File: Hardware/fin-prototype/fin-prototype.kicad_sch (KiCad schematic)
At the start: 0 parts

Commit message: setup libraries
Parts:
- added C1, C2, C4: 10 nF, Capacitor_SMD:C_0603_1608Metric, symbol Device:C_Small
- added C3, C5: 1 uF, Capacitor_SMD:C_0603_1608Metric, symbol Device:C_Small
- added C6: 220 nF, Capacitor_SMD:C_0603_1608Metric, symbol Device:C_Small
- added J10, J9: Conn_01x04_Pin, Connector_PinHeader_2.54mm:PinHeader_1x04_P2.54mm_Vertical, symbol Connector:Conn_01x04_Pin
- added R1: 10 k, Resistor_SMD:R_0603_1608Metric, symbol Device:R_US
- added R2, R3, R8, R9: 1 k, Resistor_SMD:R_0603_1608Metric, symbol Device:R_US
- added R4, R5, R6, R7: 2.5 k, Resistor_SMD:R_0603_1608Metric, symbol Device:R_US
- added U1: ADS131M03QPWRQ1, FinLib:ADS131M03, symbol FinLib:ADS131M03QPWRQ1
- added U2: TMP235A4DBZR, FinLib:TMP235A4DBZR, symbol FinLib:TMP235A4DBZR
- added U3: STM32L412KBUx, Package_DFN_QFN:QFN-32-1EP_5x5mm_P0.5mm_EP3.45x3.45mm, symbol MCU_ST_STM32L4:STM32L412KBUx
- added U4: W25N512GVEIG, FinLib:WSON8_8x6_E_WIN, symbol FinLib:W25N512GVEIG
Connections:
- new net: C4.1, R6.2, U1.7 (AIN2P)
- new net: C4.2, R7.1, U1.8 (AIN2N)
- new net: C1.1, R1.2, U1.3 (AIN0P)
- new net: C2.1, R4.2, U1.5 (AIN1N)
- new net: C2.2, R5.1, U1.6 (AIN1P)
- new net: U3.16 (VSS), U3.32 (VSS), U3.33 (VSS)
- new net: C6.1, U1.18 (CAP)
- new net +3.3V: C3.1, C5.1, J10.1 (Pin_1), J9.1 (Pin_1), R2.2, R8.1, U1.1 (AVDD), U1.20 (DVDD), U2.1 (VDD)
- new net ADCCLK: U1.17 (CLKIN)
- new net DIN: U1.16 (DIN)
- new net DOUT: U1.15 (DOUT)
- new net GAUGE1_IN_N: R2.1, R3.1, R6.1
- new net GAUGE1_IN_P: J9.2 (Pin_2), J9.3 (Pin_3), R7.2
- new net GAUGE2_IN_N: R5.2, R8.2, R9.2
- new net GAUGE2_IN_P: J10.2 (Pin_2), J10.3 (Pin_3), R4.1
- new net GND: C1.2, C3.2, C5.2, C6.2, J10.4 (Pin_4), J9.4 (Pin_4), R3.2, R9.1, U1.19 (DGND), U1.2 (AGND), U1.4 (AIN0N), U2.3 (GND)
- new net SPICLK: U1.14 (SCLK)
- new net TMP_IN_P: R1.1, U2.2 (VOUT)
- new net ~{CS}: U1.12 (*CS)
- new net ~{DRDY}: U1.13 (*DRDY)
- new net ~{SYNC}/~{RST}: U1.11 (*SYNC/*RESET)

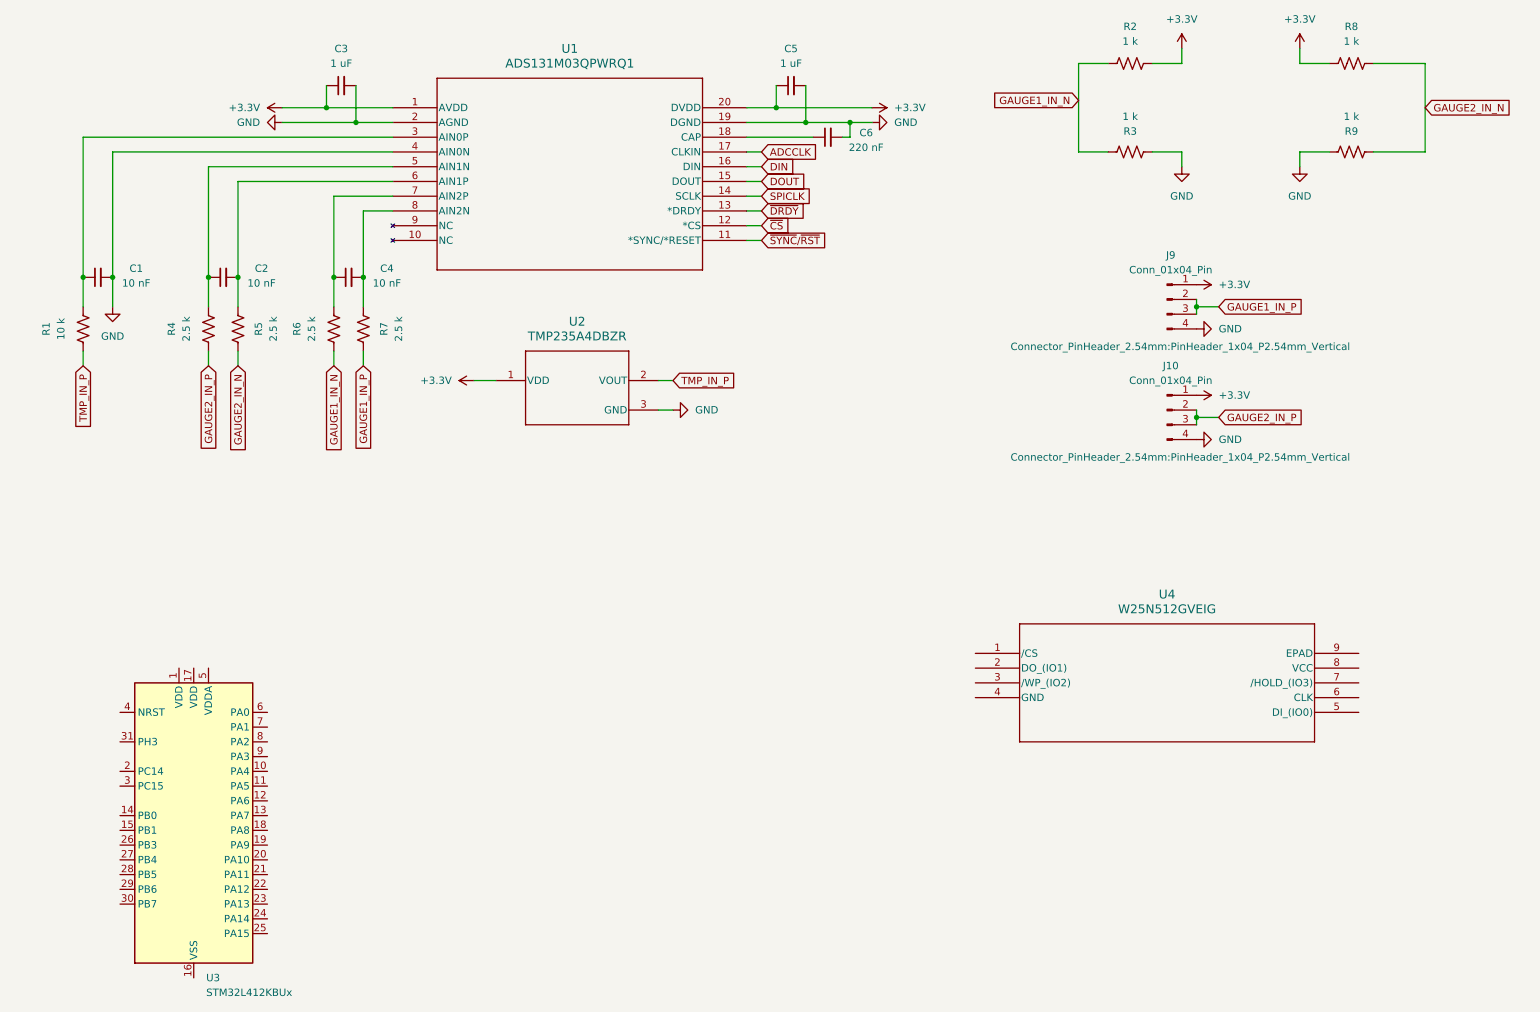
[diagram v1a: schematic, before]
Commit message: start pin assignments
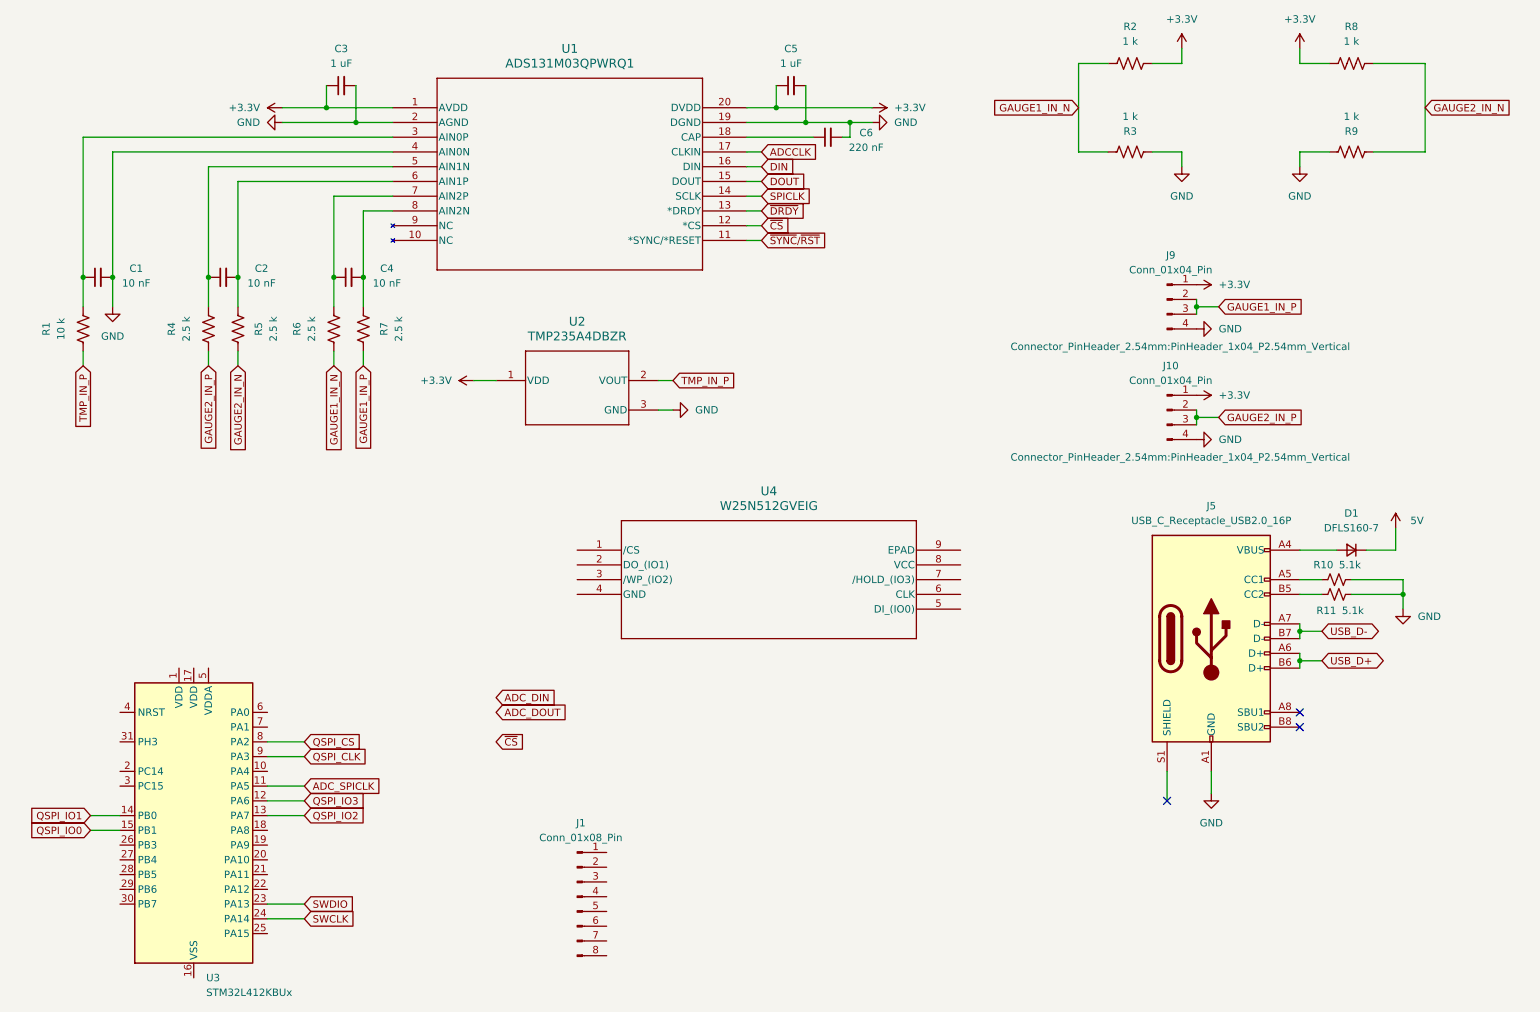
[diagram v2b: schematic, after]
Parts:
- added D1: DFLS160-7, Diode_SMD:D_PowerDI-123, symbol Device:D_Small
- added J1: Conn_01x08_Pin, symbol Connector:Conn_01x08_Pin
- added J5: USB_C_Receptacle_USB2.0_16P, Connector_USB:USB_C_Receptacle_GCT_USB4105-xx-A_16P_TopMnt_Horizontal, symbol Connector:USB_C_Receptacle_USB2.0_16P
- added R10, R11: 5.1k, Resistor_SMD:R_0402_1005Metric, symbol Device:R_Small_US
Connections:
- net GND: now also J5.A1 (GND), J5.A12 (GND), J5.B1 (GND), J5.B12 (GND), R10.2, R11.2
- net ADC_SPICLK: now reaches U3.11 (PA5)
- net QSPI_IO3: now reaches U3.12 (PA6)
- net QSPI_IO2: now reaches U3.13 (PA7)
- net QSPI_IO1: now reaches U3.14 (PB0)
- net QSPI_IO0: now reaches U3.15 (PB1)
- net SWDIO: now reaches U3.23 (PA13)
- net SWCLK: now reaches U3.24 (PA14)
- net QSPI_CS: now reaches U3.8 (PA2)
- net QSPI_CLK: now reaches U3.9 (PA3)
- new net: D1.2 (A), J5.A4 (VBUS), J5.A9 (VBUS), J5.B4 (VBUS), J5.B9 (VBUS)
- new net: J5.A5 (CC1), R10.1
- new net: J5.B5 (CC2), R11.1
- new net 5V: D1.1 (K)
- new net USB_D+: J5.A6 (D+), J5.B6 (D+)
- new net USB_D-: J5.A7 (D-), J5.B7 (D-)
- no-connect marks 0 -> 3
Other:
- moved on the sheet: U4

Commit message: finished schematic
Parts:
- removed U3: STM32L412KBUx, Package_DFN_QFN:QFN-32-1EP_5x5mm_P0.5mm_EP3.45x3.45mm, symbol MCU_ST_STM32L4:STM32L412KBUx
- added C10, C11, C12, C7, C8, C9: 100nF, Capacitor_SMD:C_0603_1608Metric, symbol Device:C_Small
- added D2, D3, D4, D5: LED, LED_SMD:LED_0603_1608Metric, symbol Device:LED
- added J2: Conn_01x04_Pin, FinLib:FlexCable, symbol Connector:Conn_01x04_Pin
- added R12, R13, R14, R15: 220 Ohms, Resistor_SMD:R_0603_1608Metric, symbol Device:R_Small_US
- added R16: 5K, Resistor_SMD:R_0603_1608Metric, symbol Device:R_Small_US
- added SW1, SW2: SW_Push, FinLib:SW_FSM2JMTR_TEC, symbol Switch:SW_Push
- added TP1, TP10, TP11, TP12, TP13, TP14, TP2, TP3, TP4, TP5, TP6, TP7, TP8, TP9: TestPoint, FinLib:TestPoint, symbol Connector:TestPoint
- added U3: FT232RNQ-REEL, FinLib:QFN32_FT232_FTD, symbol FinLib:FT232RNQ-REEL
- added U5: STM32L412C8T6, FinLib:LQFP-48, symbol FinLib:STM32L412C8T6
- J1: footprint (none) -> Connector_PinHeader_2.54mm:PinHeader_1x08_P2.54mm_Horizontal
- R10, R11: footprint Resistor_SMD:R_0402_1005Metric -> Resistor_SMD:R_0603_1608Metric
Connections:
- net DIN is gone; now on net ADC_DIN: U1.16 (DIN)
- net DOUT is gone; now on net ADC_DOUT: U1.15 (DOUT)
- net SPICLK is gone; now on net ADC_SPICLK: U1.14 (SCLK)
- net +3.3V: now also J1.7 (Pin_7), U4.8 (VCC), C10.1, C12.1, C8.2, C9.2, D4.2 (A), J2.1 (Pin_1), R12.2, R13.2, SW2.2, U3.1 (VCCIO), U5.1 (VBAT), U5.24 (VDDA/VREF+), U5.48 (VDD), U5.9 (VDDA/VREF+)
- net ADC_DIN: now also TP14.1, U5.28 (PB15)
- net ADC_DOUT: now also TP13.1, U5.27 (PB14)
- net ADC_SPICLK: now also TP12.1, U5.26 (PB13)
- net GND: now also J1.8 (Pin_8), U4.4 (GND), U4.9 (EPAD), C10.2, C11.2, C12.2, C7.2, C8.1, C9.1, J2.4 (Pin_4), R14.2, R15.2, R16.2, SW1.2, U3.17 (GND), U3.20 (GND), U3.24 (AGND), U3.26 (TEST), U3.33 (EPAD), U3.4 (GND), U5.23 (VSSA/VREF-), U5.35 (VSS), U5.47 (VSS), U5.8 (VSSA/VREF-)
- net QSPI_CLK: now also U4.6 (CLK), TP5.1, U5.13 (PA3)
- net QSPI_CS: now also U4.1 (/CS), TP4.1, U5.12 (PA2)
- net QSPI_IO0: now also U4.5 (DI_(IO0)), TP8.1, U5.19 (PB1)
- net QSPI_IO1: now also U4.2 (DO_(IO1)), TP7.1, U5.18 (PB0)
- net QSPI_IO2: now also U4.3 (/WP_(IO2)), TP6.1, U5.17 (PA7)
- net QSPI_IO3: now also U4.7 (/HOLD_(IO3)), U5.16 (PA6)
- net SWCLK: now also J1.4 (Pin_4), U5.37 (PA14)
- net SWDIO: now also J1.5 (Pin_5), U5.34 (PA13)
- net USB_D+: now also U3.14 (USBDP)
- net USB_D-: now also U3.15 (USBDM)
- net DATA_MOSI: now reaches J1.1 (Pin_1)
- net DATA_MOSI: now also U5.33 (PA12)
- net DATA_MISO: now reaches J1.2 (Pin_2)
- net DATA_MISO: now also U5.32 (PA11)
- net DATA_CS: now reaches J1.3 (Pin_3)
- net DATA_CS: now also U5.14 (PA4)
- net DATA_SCK: now reaches J1.6 (Pin_6)
- net DATA_SCK: now also U5.11 (PA1)
- net 5V renamed +5V
- net +5V: now also U3.19 (VCC)
- net ADCCLK renamed ADC_CLK
- net ADC_CLK: now also TP3.1, U5.10 (PA0)
- net ~{CS} renamed ADC_~{CS}
- net ADC_~{CS}: now also TP11.1, U5.25 (PB12)
- net ~{DRDY} renamed ADC_~{DRDY}
- net ADC_~{DRDY}: now also TP9.1, U5.45 (PB8)
- net ~{SYNC}/~{RST} renamed ADC_~{SYNC}/~{RST}
- net ADC_~{SYNC}/~{RST}: now also TP10.1, U5.46 (PB9)
- new net: C11.1, SW1.1, U5.7 (NRST)
- new net: D5.2 (A), U5.41 (PB5)
- new net: R16.1, SW2.1, U5.44 (PH3-BOOT0)
- new net: D4.1 (K), R14.1
- new net: D5.1 (K), R15.1
- new net: D2.1 (K), U3.22 (CBUS0)
- new net: D2.2 (A), R12.1
- new net: C7.1, U3.16 (3V3OUT)
- new net: D3.1 (K), U3.21 (CBUS1)
- new net: D3.2 (A), R13.1
- new net AVBAY_SYNC: J2.3 (Pin_3), U5.22 (PB11)
- new net PA15: U5.38 (PA15)
- new net PA5: U5.15 (PA5)
- new net PA8: U5.29 (PA8)
- new net PB2: U5.20 (PB2)
- new net PB3: U5.39 (PB3)
- new net PB4: U5.40 (PB4)
- new net PB6: U5.42 (PB6)
- new net PB7: U5.43 (PB7)
- new net PC13: U5.2 (PC13)
- new net PC14: U5.3 (PC14-OSC32_IN)
- new net PC15: U5.4 (PC15-OSC32_OUT)
- new net PH0: U5.5 (PH0-OSC_IN)
- new net PH1: U5.6 (PH1-OSC_OUT)
- new net SIGNAL: J2.2 (Pin_2), U5.21 (PB10)
- new net USART_RX: TP2.1, U3.30 (TXD), U5.31 (PA10)
- new net USART_TX: TP1.1, U3.2 (RXD), U5.30 (PA9)
- no-connect marks 3 -> 16
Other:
- note added: "Note: CLK uses TIM2_CH1 pin, ensure ETR pins aren't needed for anything"
- note added: "Potentially Change Strain Gauge to JST"
- moved on the sheet: C1, C2, C3, C4, C5, C6, D1, J1, J10, J5, J9, R1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

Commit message: prettify schematic a bit
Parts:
- removed C10, C11: 100nF, Capacitor_SMD:C_0603_1608Metric, symbol Device:C_Small
- removed D5: LED, LED_SMD:LED_0603_1608Metric, symbol Device:LED
- removed R13, R15: 220 Ohms, Resistor_SMD:R_0603_1608Metric, symbol Device:R_Small_US
- removed R16: 5K, Resistor_SMD:R_0603_1608Metric, symbol Device:R_Small_US
- removed U5: STM32L412C8T6, FinLib:LQFP-48, symbol FinLib:STM32L412C8T6
- added C2, C6, C7: 100nF, Capacitor_SMD:C_0603_1608Metric, symbol Device:C_Small
- added D4: LED, LED_SMD:LED_0603_1608Metric, symbol Device:LED
- added J10, J11, J12, J13, J14, J15, J16, J17, J18, J6, J7, J8, J9: Conn_01x01_Pin, Connector_PinHeader_2.54mm:PinHeader_1x01_P2.54mm_Vertical, symbol Connector:Conn_01x01_Pin
- added R10, R9: 220, Resistor_SMD:R_0603_1608Metric, symbol Device:R_Small_US
- added R2: 5K, Resistor_SMD:R_0603_1608Metric, symbol Device:R_Small_US
- added TP15, TP16, TP17, TP18, TP19, TP20, TP21: TestPoint, FinLib:TestPoint, symbol Connector:TestPoint
- added U2: STM32L412C8Tx, Package_QFP:LQFP-48_7x7mm_P0.5mm, symbol MCU_ST_STM32L4:STM32L412C8Tx
- R7: renamed from R14; value 220 Ohms -> 220
- R8: renamed from R12; value 220 Ohms -> 220
- TP1, TP2, TP3, TP4: footprint FinLib:TestPoint -> TestPoint:TestPoint_Loop_D1.80mm_Drill1.0mm_Beaded
- renumbered C5 to C10, C6 to C11, C7 to C13, C2 to C3, C3 to C4, C4 to C5, D4 to D1, D1 to D5, J5 to J1, J9 to J2, J10 to J3, J1 to J4, J2 to J5, R2 to R11, R3 to R12, R8 to R13, R9 to R14, R10 to R15, R11 to R16, R4 to R3, R5 to R4, R6 to R5, R7 to R6, U4 to U3, U2 to U4, U3 to U5
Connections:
- net DATA_SCK is gone; now on net SWCLK: J4.6 (Pin_6)
- net +3.3V: now also C4.2, C8.1, C9.1, D2.2 (A), D3.2 (A), SW2.1, C6.1, C7.1, U2.1 (VBAT), U2.24 (VDD), U2.48 (VDD), U2.9 (VDDA); no longer C4.1, C8.2, C9.2, R8.2, SW2.2
- net ADC_~{SYNC}/~{RST}: now also U2.46 (PB9)
- net AVBAY_SYNC: now also U2.22 (PB11)
- net GND: now also C4.1, C8.2, C9.2, SW1.1, TP1.1, TP2.1, TP3.1, TP4.1, C2.1, C6.2, C7.2, R10.1, R2.1, U2.23 (VSS), U2.35 (VSS), U2.47 (VSS), U2.8 (VSSA); no longer C4.2, C8.1, C9.1, SW1.2
- net PA15: now also J8.1 (Pin_1), U2.38 (PA15)
- net PA5: now also J6.1 (Pin_1), U2.15 (PA5)
- net PA8: now also J7.1 (Pin_1), U2.29 (PA8)
- net PB2: now also J9.1 (Pin_1), U2.20 (PB2)
- net PB3: now also J10.1 (Pin_1), U2.39 (PB3)
- net PB4: now also J11.1 (Pin_1), U2.40 (PB4)
- net PB6: now also J12.1 (Pin_1), U2.42 (PB6)
- net PB7: now also J13.1 (Pin_1), U2.43 (PB7)
- net PC13: now also J14.1 (Pin_1), U2.2 (PC13)
- net PC14: now also J15.1 (Pin_1), U2.3 (PC14)
- net PC15: now also J16.1 (Pin_1), U2.4 (PC15)
- net PH0: now also J17.1 (Pin_1), U2.5 (PH0)
- net PH1: now also J18.1 (Pin_1), U2.6 (PH1)
- net QSPI_CLK: now also TP12.1, U2.13 (PA3); no longer TP5.1
- net QSPI_IO0: now also TP13.1, U2.19 (PB1); no longer TP8.1
- net QSPI_IO1: now also TP14.1, U2.18 (PB0); no longer TP7.1
- net QSPI_IO2: now also TP15.1, U2.17 (PA7); no longer TP6.1
- net QSPI_IO3: now also TP16.1, U2.16 (PA6)
- net SIGNAL: now also U2.21 (PB10)
- net SWCLK: now also U2.37 (PA14); no longer J4.4 (Pin_4)
- net SWDIO: now also U2.34 (PA13)
- net USB_D+: now also TP20.1
- net USB_D-: now also TP21.1
- net at D2.1 (K): now also R8.2; no longer U5.22 (CBUS0)
- net ~{TX_LED}: now reaches R8.1
- net ~{TX_LED}: now also U5.22 (CBUS0); no longer D2.2 (A)
- net at D3.1 (K): now also R9.2; no longer U5.21 (CBUS1)
- net ADC_CLK renamed TIM2_CH1
- net TIM2_CH1: now also TP9.1, U2.10 (PA0); no longer TP3.1
- net ADC_DIN renamed SPI2_MOSI
- net SPI2_MOSI: now also TP7.1, U2.28 (PB15); no longer TP14.1
- net ADC_DOUT renamed SPI2_MISO
- net SPI2_MISO: now also TP6.1, U2.27 (PB14); no longer TP13.1
- net ADC_SPICLK renamed SPI2_SCK
- net SPI2_SCK: now also TP5.1, U2.26 (PB13); no longer TP12.1
- net ADC_~{CS} renamed ~{ADC_CS}
- net ~{ADC_CS}: now also TP8.1, U2.25 (PB12); no longer TP11.1
- net ADC_~{DRDY} renamed ~{ADC_DRDY}
- net ~{ADC_DRDY}: now also TP11.1, U2.45 (PB8); no longer TP9.1
- net DATA_CS renamed ~{SPI1_CS}
- net ~{SPI1_CS}: now also U2.14 (PA4)
- net DATA_MISO renamed SPI1_MISO
- net SPI1_MISO: now also U2.32 (PA11)
- net DATA_MOSI renamed SPI1_MOSI
- net SPI1_MOSI: now also U2.33 (PA12)
- net QSPI_CS renamed ~{FLASH_CS}
- net ~{FLASH_CS}: now also TP17.1, U2.12 (PA2); no longer TP4.1
- net USART_RX renamed USART1_RX
- net USART1_RX: now also TP18.1, U2.31 (PA10); no longer TP2.1
- net USART_TX renamed USART1_TX
- net USART1_TX: now also TP19.1, U2.30 (PA9); no longer TP1.1
- new net: D4.1 (K), R10.2
- new net: R2.2, SW2.2, U2.44 (PH3)
- new net: C2.2, SW1.2, U2.7 (NRST)
- new net SPI1_SCK: J4.4 (Pin_4), U2.11 (PA1)
- new net STATUS_LED: D4.2 (A), U2.41 (PB5)
- new net ~{RX_LED}: R9.1, U5.21 (CBUS1)
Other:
- note added: "ADC"
- note added: "AvBay"
- note added: "External Connections"
- note added: "Extra MCU Pins"
- note added: "Flash"
- note added: "LEDs"
- note added: "Programming/Postflight Data"
- note added: "STM32L4"
- note added: "Sensing"
- note added: "Strain Gauges"
- note added: "Test Points"
- note added: "USB"
- note removed: "Note: CLK uses TIM2_CH1 pin, ensure ETR pins aren't needed for anything"
- note removed: "Potentially Change Strain Gauge to JST"
- moved on the sheet: C1, C10, C11, C12, C13, C3, C4, C5, D1, D2, D5, J1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

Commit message: start placing components
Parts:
- J4: footprint Connector_PinHeader_2.54mm:PinHeader_1x08_P2.54mm_Horizontal -> Connector_PinHeader_2.54mm:PinHeader_1x08_P2.54mm_Vertical
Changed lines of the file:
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@@
 	(wire
 		(pts
-			(xy 217.17 127) (xy 217.17 121.92)
-		)
-		(stroke
-			(width 0)
-			(type default)
-		)
-	)
-	(wire
-		(pts
 			(xy 25.4 64.77) (xy 25.4 69.85)
 		)
@@
 	(wire
 		(pts
+			(xy 217.17 127) (xy 218.44 127)
+		)
+		(stroke
+			(width 0)
+			(type default)
+		)
+	)
+	(wire
+		(pts
 			(xy 334.01 224.79) (xy 337.82 224.79)
 		)
@@
 	(wire
 		(pts
-			(xy 217.17 121.92) (xy 220.98 121.92)
-		)
-		(stroke
-			(width 0)
-			(type default)
-		)
-	)
-	(wire
-		(pts
 			(xy 229.87 87.63) (xy 229.87 88.9)
 		)
@@
 	(wire
 		(pts
-			(xy 220.98 121.92) (xy 220.98 123.19)
+			(xy 292.1 81.28) (xy 295.91 81.28)
 		)
 		(stroke
@@
 	(wire
 		(pts
-			(xy 292.1 81.28) (xy 295.91 81.28)
+			(xy 63.5 144.78) (xy 68.58 144.78)
 		)
 		(stroke
@@
 	(wire
 		(pts
-			(xy 63.5 144.78) (xy 68.58 144.78)
+			(xy 218.44 127) (xy 218.44 139.7)
 		)
 		(stroke
@@
 			)
 		)
-		(property "Footprint" "Connector_PinHeader_2.54mm:PinHeader_1x08_P2.54mm_Horizontal"
+		(property "Footprint" "Connector_PinHeader_2.54mm:PinHeader_1x08_P2.54mm_Vertical"
 			(at 287.02 83.82 0)
 			(effects
@@
 	(symbol
 		(lib_id "power:GND")
-		(at 220.98 123.19 0)
+		(at 218.44 139.7 0)
 		(unit 1)
 		(exclude_from_sim no)
@@
 		(fields_autoplaced yes)
 		(property "Reference" "#PWR021"
-			(at 220.98 129.54 0)
+			(at 218.44 146.05 0)
 			(effects
 				(font
@@
 		)
 		(property "Value" "GND"
-			(at 223.52 124.4599 0)
+			(at 220.98 140.9699 0)
 			(effects
 				(font
@@
 		)
 		(property "Footprint" ""
-			(at 220.98 123.19 0)
+			(at 218.44 139.7 0)
 			(effects
 				(font
@@
 		)
 		(property "Datasheet" ""
-			(at 220.98 123.19 0)
+			(at 218.44 139.7 0)
 			(effects
 				(font
@@
 		)
 		(property "Description" "Power symbol creates a global label with name \"GND\" , ground"
-			(at 220.98 123.19 0)
+			(at 218.44 139.7 0)
 			(effects
 				(font

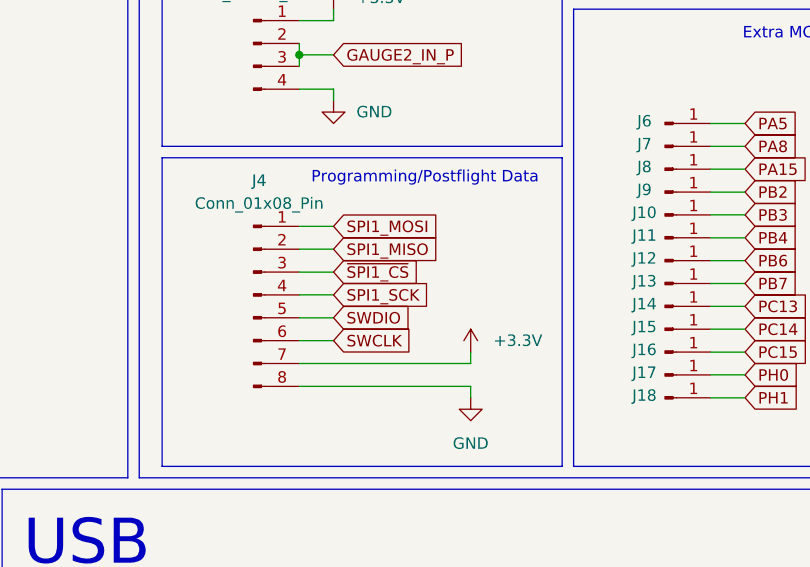
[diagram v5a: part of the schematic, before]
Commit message: all traces but test points
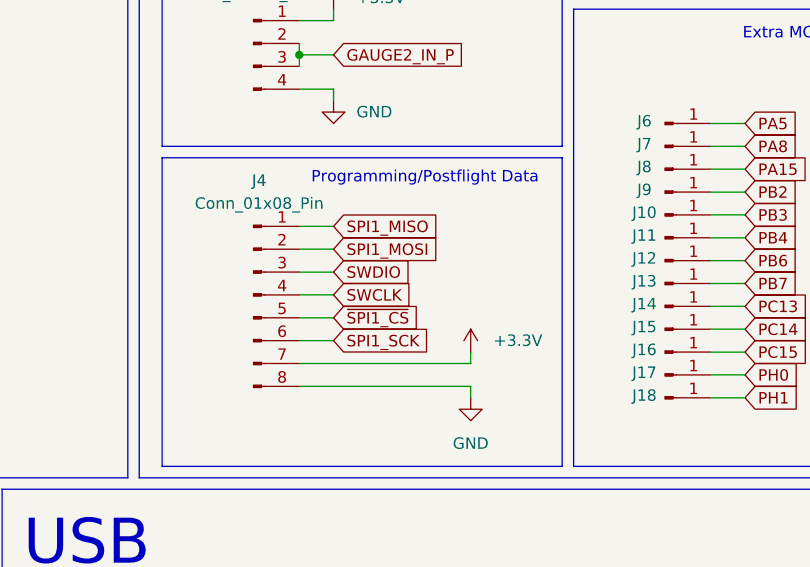
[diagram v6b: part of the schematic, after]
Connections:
- net SPI1_MISO: now also J4.1 (Pin_1); no longer J4.2 (Pin_2)
- net SPI1_MOSI: now also J4.2 (Pin_2); no longer J4.1 (Pin_1)
- net SPI1_SCK: now also J4.6 (Pin_6); no longer J4.4 (Pin_4)
- net SWCLK: now also J4.4 (Pin_4); no longer J4.6 (Pin_6)
- net SWDIO: now also J4.3 (Pin_3); no longer J4.5 (Pin_5)
- net ~{SPI1_CS}: now also J4.5 (Pin_5); no longer J4.3 (Pin_3)
